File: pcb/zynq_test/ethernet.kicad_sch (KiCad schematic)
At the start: 62 parts, among them J1101 RJ45_JK0654219, Q1101 FDY102PZ, Q1102 NMOS, Q1103 NMOS, U1101 DSC1001CI2-025, U1102 LAN8830

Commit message: Finished Power Supply
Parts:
- removed Q1102, Q1103: NMOS, symbol Simulation_SPICE:NMOS
- added Q1102, Q1103: 2N7002E, Package_TO_SOT_SMD:SOT-23, symbol Transistor_FET:2N7002E
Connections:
- net GND: now also Q1102.2 (S), Q1103.2 (S)
- net LED1_D: now also Q1102.1 (G)
- net LED2_D: now also Q1103.1 (G)
- net at R1126.2: now also Q1103.3 (D)
- net at R1122.2: now also Q1102.3 (D)
- net +3.3V renamed +3V3
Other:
- title: (none) -> Ethernet
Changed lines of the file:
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@@
 	(paper "A4")
 	(title_block
-		(date "2025-09-06")
-		(rev "v1.0")
+		(title "Ethernet")
+		(date "2025-09-13")
+		(rev "A")
 	)
 	(rectangle
@@
 	)
 	(label "ETH_1V1"
-		(at 153.67 158.75 0)
+		(at 152.4 158.75 180)
 		(effects
 			(font
 				(size 1.27 1.27)
 			)
-			(justify left bottom)
+			(justify right bottom)
 		)
 	)
@@
 			)
 		)
-		(property "Value" "+3.3V"
+		(property "Value" "+3V3"
 			(at 244.602 24.638 0)
 			(effects
@@
 	)
 	(symbol
-		(lib_id "Simulation_SPICE:NMOS")
-		(at 264.16 119.38 0)
+		(lib_id "Transistor_FET:2N7002E")
+		(at 236.22 119.38 0)
 		(unit 1)
 		(exclude_from_sim no)
@@
 		(dnp no)
 		(fields_autoplaced yes)
-		(property "Reference" "Q1103"
-			(at 270.51 118.1099 0)
+		(property "Reference" "Q1102"
+			(at 242.57 118.1099 0)
 			(effects
 				(font
@@
 			)
 		)
-		(property "Value" "NMOS"
-			(at 270.51 120.6499 0)
+		(property "Value" "2N7002E"
+			(at 242.57 120.6499 0)
 			(effects
 				(font
@@
 			)
 		)
-		(property "Footprint" ""
-			(at 269.24 116.84 0)
-			(effects
-				(font
-					(size 1.27 1.27)
-				)
-				(hide yes)
-			)
-		)
-		(property "Datasheet" "https://ngspice.sourceforge.io/docs/ngspice-html-manual/manual.xhtml#cha_MOSFETs"
-			(at 264.16 132.08 0)
-			(effects
-				(font
-					(size 1.27 1.27)
-				)
-				(hide yes)
-			)
-		)
-		(property "Description" "N-MOSFET transistor, drain/source/gate"
-			(at 264.16 119.38 0)
-			(effects
-				(font
-					(size 1.27 1.27)
-				)
-				(hide yes)
-			)
-		)
-		(property "Sim.Device" "NMOS"
-			(at 264.16 136.525 0)
+		(property "Footprint" "Package_TO_SOT_SMD:SOT-23"
+			(at 241.3 121.285 0)
 			(effects
 				(font
 					(size 1.27 1.27)
+					(italic yes)
 				)
+				(justify left)
 				(hide yes)
 			)
 		)
-		(property "Sim.Type" "VDMOS"
-			(at 264.16 138.43 0)
+		(property "Datasheet" "http://www.diodes.com/assets/Datasheets/ds30376.pdf"
+			(at 241.3 123.19 0)
 			(effects
 				(font
 					(size 1.27 1.27)
 				)
+				(justify left)
 				(hide yes)
 			)
 		)
-		(property "Sim.Pins" "1=D 2=G 3=S"
-			(at 264.16 134.62 0)
+		(property "Description" "0.24A Id, 60V Vds, N-Channel MOSFET, SOT-23"
+			(at 236.22 119.38 0)
 			(effects
 				(font
@@
 			)
 		)
-		(pin "2"
-		)
 		(pin "3"
 		)
 		(pin "1"
 		)
+		(pin "2"
+		)
 		(instances
-			(project ""
+			(project "zynq_test"
 				(path "/0637578d-4ce5-4d31-b973-2de977269ea5/c2781f92-5ea5-4e37-80b2-cda210986130"
-					(reference "Q1103")
+					(reference "Q1102")
 					(unit 1)
 				)
@@
 			)
 		)
-		(property "Value" "+3.3V"
+		(property "Value" "+3V3"
 			(at 65.278 106.68 0)
 			(effects
@@
 	)
 	(symbol
-		(lib_id "Simulation_SPICE:NMOS")
-		(at 236.22 119.38 0)
-		(unit 1)
-		(exclude_from_sim no)
-		(in_bom yes)
-		(on_board yes)
-		(dnp no)
-		(fields_autoplaced yes)
-		(property "Reference" "Q1102"
-			(at 242.57 118.1099 0)
-			(effects
-				(font
-					(size 1.27 1.27)
-				)
-				(justify left)
-			)
-		)
-		(property "Value" "NMOS"
-			(at 242.57 120.6499 0)
-			(effects
-				(font
-					(size 1.27 1.27)
-				)
-				(justify left)
-			)
-		)
-		(property "Footprint" ""
-			(at 241.3 116.84 0)
-			(effects
-				(font
-					(size 1.27 1.27)
-				)
-				(hide yes)
-			)
-		)
-		(property "Datasheet" "https://ngspice.sourceforge.io/docs/ngspice-html-manual/manual.xhtml#cha_MOSFETs"
-			(at 236.22 132.08 0)
-			(effects
-				(font
-					(size 1.27 1.27)
-				)
-				(hide yes)
-			)
-		)
-		(property "Description" "N-MOSFET transistor, drain/source/gate"
-			(at 236.22 119.38 0)
-			(effects
-				(font
-					(size 1.27 1.27)
-				)
-				(hide yes)
-			)
-		)
-		(property "Sim.Device" "NMOS"
-			(at 236.22 136.525 0)
-			(effects
-				(font
-					(size 1.27 1.27)
-				)
-				(hide yes)
-			)
-		)
-		(property "Sim.Type" "VDMOS"
-			(at 236.22 138.43 0)
-			(effects
-				(font
-					(size 1.27 1.27)
-				)
-				(hide yes)
-			)
-		)
-		(property "Sim.Pins" "1=D 2=G 3=S"
-			(at 236.22 134.62 0)
-			(effects
-				(font
-					(size 1.27 1.27)
-				)
-				(hide yes)
-			)
-		)
-		(pin "2"
-		)
-		(pin "3"
-		)
-		(pin "1"
-		)
-		(instances
-			(project "zynq_test"
-				(path "/0637578d-4ce5-4d31-b973-2de977269ea5/c2781f92-5ea5-4e37-80b2-cda210986130"
-					(reference "Q1102")
-					(unit 1)
-				)
-			)
-		)
-	)
-	(symbol
 		(lib_id "power:GND")
 		(at 133.35 166.37 0)
@@
 			)
 		)
-		(property "Value" "+3.3V"
+		(property "Value" "+3V3"
 			(at 149.352 140.208 0)
 			(effects
@@
 	)
 	(symbol
+		(lib_id "Transistor_FET:2N7002E")
+		(at 264.16 119.38 0)
+		(unit 1)
+		(exclude_from_sim no)
+		(in_bom yes)
+		(on_board yes)
+		(dnp no)
+		(fields_autoplaced yes)
+		(property "Reference" "Q1103"
+			(at 270.51 118.1099 0)
+			(effects
+				(font
+					(size 1.27 1.27)
+				)
+				(justify left)
+			)
+		)
+		(property "Value" "2N7002E"
+			(at 270.51 120.6499 0)
+			(effects
+				(font
+					(size 1.27 1.27)
+				)
+				(justify left)
+			)
+		)
+		(property "Footprint" "Package_TO_SOT_SMD:SOT-23"
+			(at 269.24 121.285 0)
+			(effects
+				(font
+					(size 1.27 1.27)
+					(italic yes)
+				)
+				(justify left)
+				(hide yes)
+			)
+		)
+		(property "Datasheet" "http://www.diodes.com/assets/Datasheets/ds30376.pdf"
+			(at 269.24 123.19 0)
+			(effects
+				(font
+					(size 1.27 1.27)
+				)
+				(justify left)
+				(hide yes)
+			)
+		)
+		(property "Description" "0.24A Id, 60V Vds, N-Channel MOSFET, SOT-23"
+			(at 264.16 119.38 0)
+			(effects
+				(font
+					(size 1.27 1.27)
+				)
+				(hide yes)
+			)
+		)
+		(pin "3"
+		)
+		(pin "1"
+		)
+		(pin "2"
+		)
+		(instances
+			(project "zynq_test"
+				(path "/0637578d-4ce5-4d31-b973-2de977269ea5/c2781f92-5ea5-4e37-80b2-cda210986130"
+					(reference "Q1103")
+					(unit 1)
+				)
+			)
+		)
+	)
+	(symbol
 		(lib_id "power:GND")
 		(at 76.2 179.07 0)
@@
 			)
 		)
-		(property "Value" "+3.3V"
+		(property "Value" "+3V3"
 			(at 245.364 71.882 0)
 			(effects
@@
 			)
 		)
-		(property "Value" "+3.3V"
+		(property "Value" "+3V3"
 			(at 44.196 144.526 0)
 			(effects

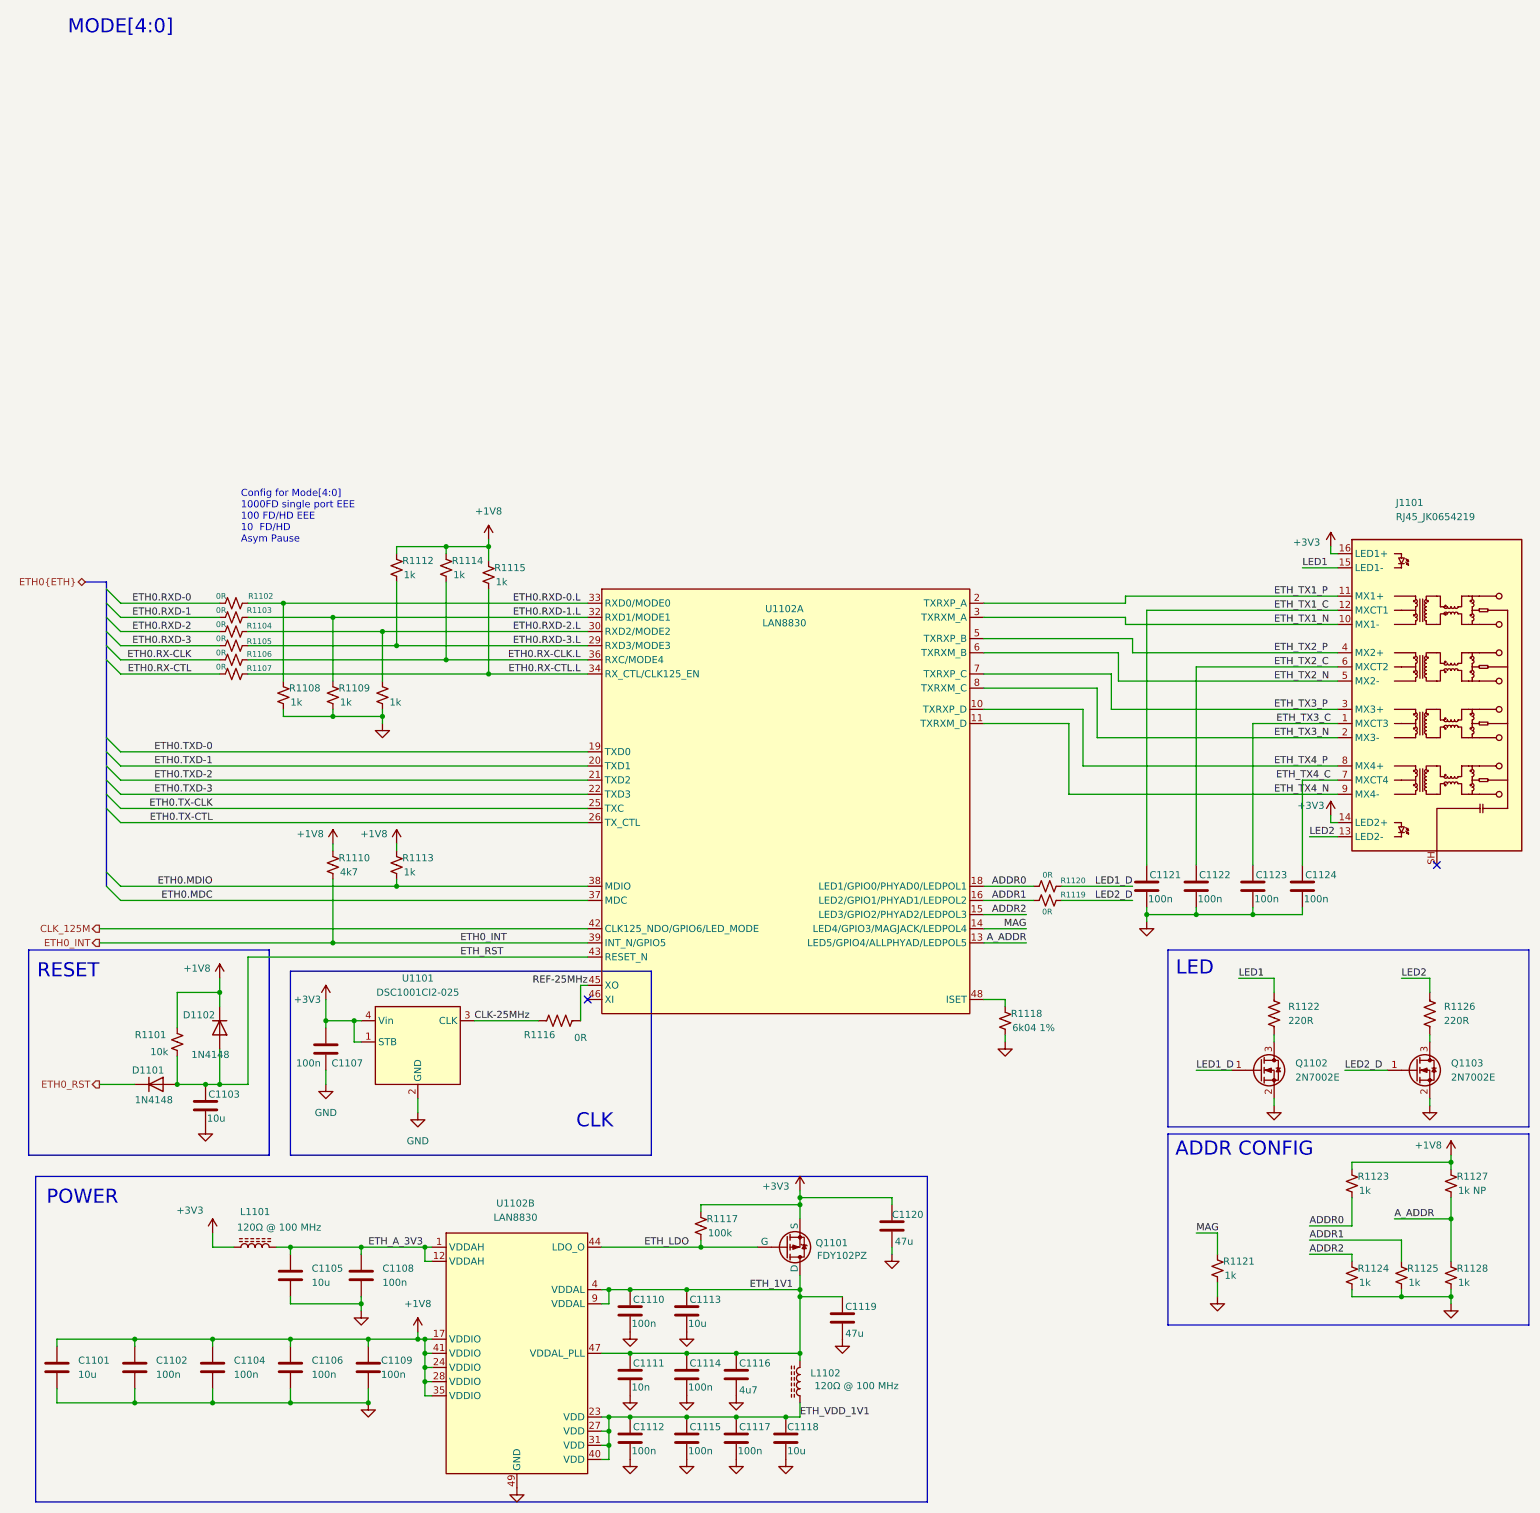
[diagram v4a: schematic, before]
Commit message: Finished most of the schematic, will start routing soon
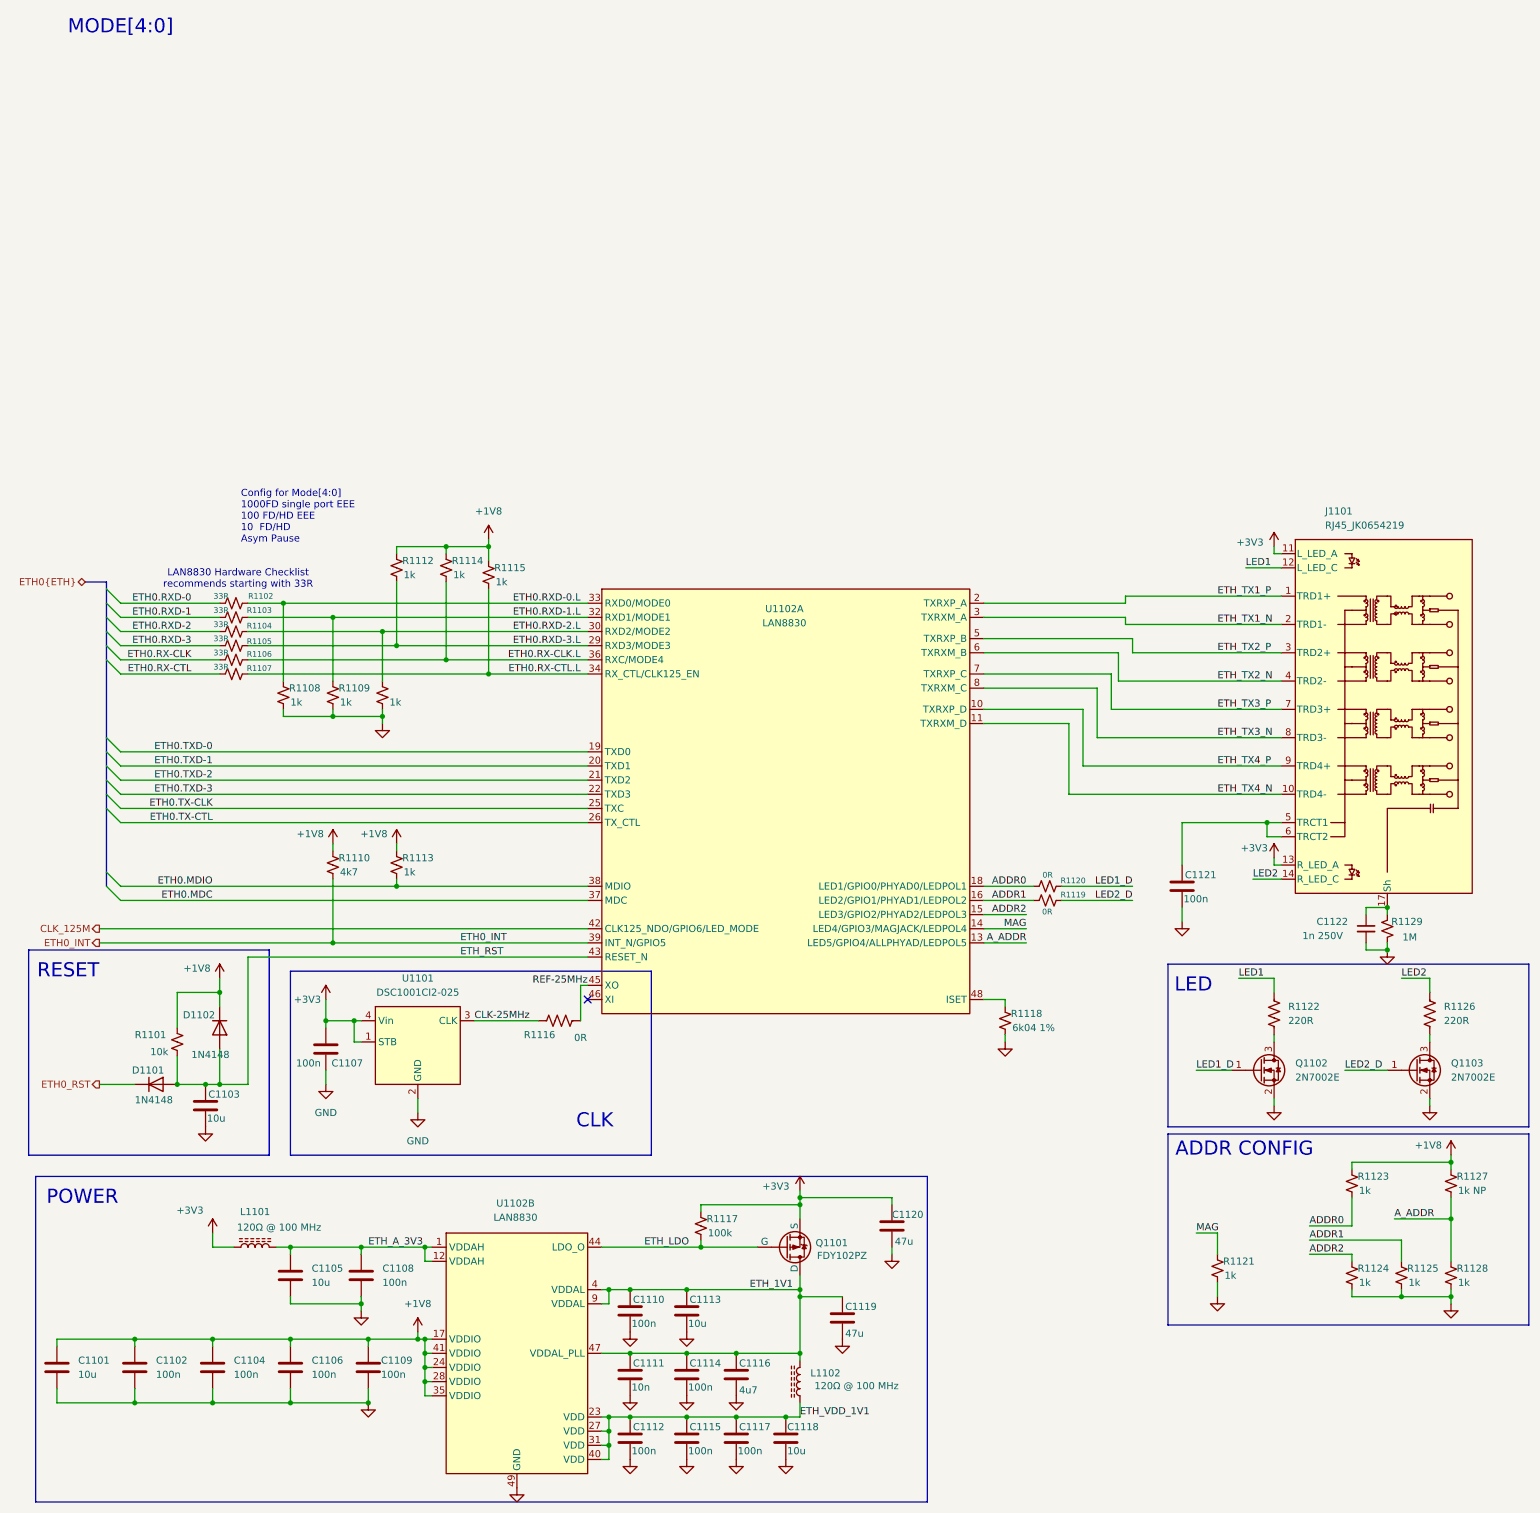
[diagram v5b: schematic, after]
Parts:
- removed C1122, C1123, C1124: 100n, symbol Device:C
- added C1122: 1n 250V, symbol Device:C_Small
- added R1129: 1M, symbol Device:R_Small_US
- J1101: footprint Connector_RJ:RJ45_Pulse_JK0654219NL_Horizontal -> ARJM11C7-502-AB-ER2-T_ABR; symbol Connector:RJ45_JK0654219 -> ethernetJack:ARJM11C7-502-AB-ER2-T
- R1102, R1103, R1104, R1105, R1106, R1107: value 0R -> 33R
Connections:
- net ETH_TX2_C is gone; now on an unnamed net: J1101.6 (TRCT2)
- net ETH_TX3_C is gone; now on net ETH_TX1_P: J1101.1 (TRD1+)
- net ETH_TX4_C is gone; now on net ETH_TX3_P: J1101.7 (TRD3+)
- net +3V3: now also J1101.11 (L_LED_A), J1101.13 (R_LED_A); no longer J1101.14 (LED2+), J1101.16 (LED1+)
- net ETH_TX1_N: now also J1101.2 (TRD1-); no longer J1101.10 (MX1-)
- net ETH_TX1_P: no longer J1101.11 (MX1+)
- net ETH_TX2_N: now also J1101.4 (TRD2-); no longer J1101.5 (MX2-)
- net ETH_TX2_P: now also J1101.3 (TRD2+); no longer J1101.4 (MX2+)
- net ETH_TX3_N: now also J1101.8 (TRD3-); no longer J1101.2 (MX3-)
- net ETH_TX3_P: no longer J1101.3 (MX3+)
- net ETH_TX4_N: now also J1101.10 (TRD4-); no longer J1101.9 (MX4-)
- net ETH_TX4_P: now also J1101.9 (TRD4+); no longer J1101.8 (MX4+)
- net GND: now also C1122.2, R1129.2
- net LED1: now also J1101.12 (L_LED_C); no longer J1101.15 (LED1-)
- net LED2: now also J1101.14 (R_LED_C); no longer J1101.13 (LED2-)
- net ETH_TX1_C: no longer names the net of C1121.1
- net ETH_TX1_C: now also J1101.5 (TRCT1); no longer J1101.12 (MXCT1)
- new net: C1122.1, J1101.17 (Sh), J1101.18 (Sh), R1129.1
- no-connect marks 2 -> 1
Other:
- note added: "LAN8830 Hardware Checklist recommends starting with 33R"
- moved on the sheet: C1121

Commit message: Finished to first ddr ic
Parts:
- J1101: footprint ARJM11C7-502-AB-ER2-T_ABR -> ethernet:ARJM11C7-502-AB-ER2-T_ABR
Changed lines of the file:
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@@
 			)
 		)
-		(property "Footprint" "ARJM11C7-502-AB-ER2-T_ABR"
+		(property "Footprint" "ethernet:ARJM11C7-502-AB-ER2-T_ABR"
 			(at 255.778 14.986 0)
 			(effects
